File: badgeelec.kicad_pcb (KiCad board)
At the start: 2 copper layers, 44.9 x 43.2 mm, 29 parts, among them J1 PROG_CONN, U1 PIC16F716-I-SO-ND, U2 TSSP58038

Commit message: additional details
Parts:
- moved C1 61.5 mm to (159.4, 100.3)
- moved C2 61.5 mm to (159.4, 104.1)
- moved C3 61.5 mm to (131.4, 106.0)
- moved D1 61.5 mm to (157.5, 81.3)
- moved D3 61.5 mm to (157.5, 85.1)
- moved D5 61.5 mm to (141.6, 81.3)
- moved D7 61.5 mm to (141.6, 85.1)
- moved R1 61.5 mm to (157.5, 91.4)
- moved R4 61.5 mm to (145.4, 91.4)
- moved U2 61.5 mm to (135.9, 109.2)
- moved BT1 61.5 mm to (151.9, 96.5)
- moved D2 61.5 mm to (162.6, 81.3)
- moved D4 61.5 mm to (162.6, 85.1)
- moved D6 61.5 mm to (146.7, 81.3)
- moved D8 61.5 mm to (146.7, 85.1)
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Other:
- board text added: "r1"

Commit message: Halfway through v2
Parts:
- added C4, C5: 18pF, Capacitors_SMD:C_0805, F.Cu at (151.4, 128.2)
- added D10: LED, LEDs:LED_1206, F.Cu at (151.4, 128.2)
- added R6: 220, Resistors_SMD:R_0805_HandSoldering, F.Cu at (151.4, 128.2)
- added Y1: 4Mhz, Crystals:Crystal_HC49-U_Vertical, F.Cu at (162.2, 109.8)
- moved G*** 36.5 mm to (133.2, 90.0)
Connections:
- U1 pad 10: /RB4 -> (no net)
- U1 pad 11: /RB5 -> (no net)
- U1 pad 3: Net-(U1-Pad3) -> (no net)
- U1 pad 9: /RB3 -> (no net)

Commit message: Implemented prototypev2
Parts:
- removed D10: LED, LEDs:LED_1206
- removed the G*** at (133.2, 90.0)
- removed JP1: permit operation / !program, Oddities:NetTie-I_SMD
- removed R6: 220, Resistors_SMD:R_0805_HandSoldering
- removed the REF** at (170.2, 78.7)
- removed the REF** at (170.2, 114.3)
- removed the REF** at (132.7, 78.7)
- removed the REF** at (132.7, 114.3)
- added G***: LOGO, 0gbadge-2018:g22ml_small, F.Cu at (141.2, 113.8)
- added J2: PWR_CONN, Pin_Headers:Pin_Header_Straight_1x02_Pitch2.54mm, F.Cu at (153.5, 129.0)
- added REF**: MountingHole_5.5mm, Mounting_Holes:MountingHole_5.5mm, F.Cu at (151.9, 72.4)
- added REF**: MountingHole_3.2mm_M3_Pad_Via, Mounting_Holes:MountingHole_3.2mm_M3_Pad_Via, F.Cu at (170.8, 118.9)
- added REF**: MountingHole_3.2mm_M3_Pad_Via, Mounting_Holes:MountingHole_3.2mm_M3_Pad_Via, F.Cu at (132.8, 118.9)
- added REF**: MountingHole_3.2mm_M3_Pad_Via, Mounting_Holes:MountingHole_3.2mm_M3_Pad_Via, F.Cu at (170.8, 81.5)
- added REF**: MountingHole_3.2mm_M3_Pad_Via, Mounting_Holes:MountingHole_3.2mm_M3_Pad_Via, F.Cu at (132.8, 81.5)
- C2: value 4.7uF -> 1uF; moved to B.Cu
- C3: value 100nF -> 10nF
- R7: value 1K -> 33K; moved to F.Cu
- Y1: footprint Crystals:Crystal_HC49-U_Vertical -> 0gbadge-2018:ABLS-4MHZ-B2-T
- moved C5 38.2 mm to (171.9, 96.0), turned to 90 degrees
- moved C4 34.9 mm to (164.9, 96.0), turned to 90 degrees
- moved C2 27.5 mm to (135.4, 90.7), turned to 270 degrees
- moved R7 17.8 mm to (132.2, 102.4), turned to 90 degrees
- moved U2 13.6 mm to (138.6, 122.5)
- moved Y1 10.6 mm to (167.4, 100.5)
- moved S1 8.52 mm to (126.9, 101.8), turned to 270 degrees
- moved J1 8.26 mm to (177.9, 99.4)
- moved BT1 7.12 mm to (152.1, 89.4)
- moved D9 5.19 mm to (157.0, 118.8)
- moved C3 5.09 mm to (126.9, 108.2), turned to 0 degrees
- moved C1 5.07 mm to (162.7, 104.2)
- moved R8 4.19 mm to (150.7, 117.5)
- moved R2 3.94 mm to (144.3, 91.2)
- moved R3 3.32 mm to (159.2, 91.2)
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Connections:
- R7 pad 2: Net-(JP1-Pad2) -> /~MCLR
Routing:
- net VDD: track 122.0 -> 170.5 mm, vias 6 -> 8
- net GND: track 38.9 -> 9.95 mm, vias 9 -> 5
- net Net-(C5-Pad1): track 0.00 -> 20.2 mm
- net /~MCLR: track 52.9 -> 67.1 mm, vias 3 -> 1
- net Net-(U1-Pad6): track 11.3 -> 23.0 mm
- net Net-(C4-Pad1): track 0.00 -> 11.2 mm
- net Net-(JP1-Pad2): track 9.76 -> 0.00 mm
- net /RB6: track 16.3 -> 22.5 mm
- net /RA1: track 13.2 -> 7.56 mm
- net /RB7: track 16.8 -> 22.0 mm
- net /RB2: track 7.69 -> 10.6 mm
- net Net-(D2-Pad1): track 9.79 -> 12.2 mm
- net /RA0: track 13.2 -> 11.1 mm
- net /RA3: track 10.3 -> 11.2 mm
- net /RA2: track 8.53 -> 7.83 mm
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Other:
- board size 44.9 x 43.2 mm -> 62.5 x 62.5 mm
- board text added: "0x0G prototype Revision 2"
- board text added: "RESET"
- board text removed: "0x0G electrical prototype"
- board text removed: "r1"

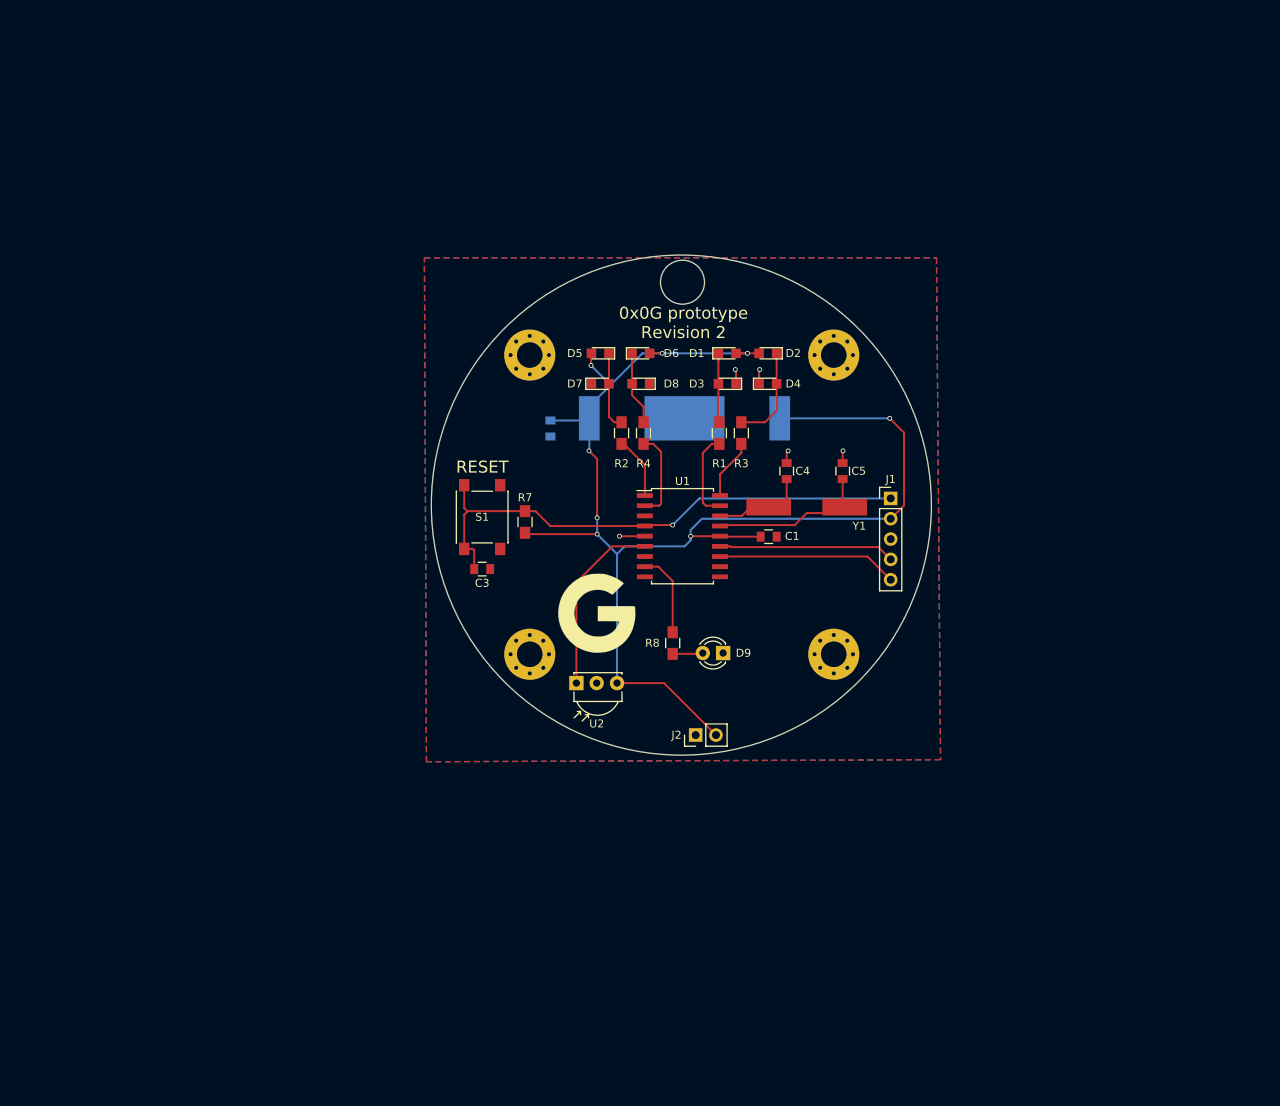
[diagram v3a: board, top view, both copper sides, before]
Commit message: Start working on layout for final prototype 1
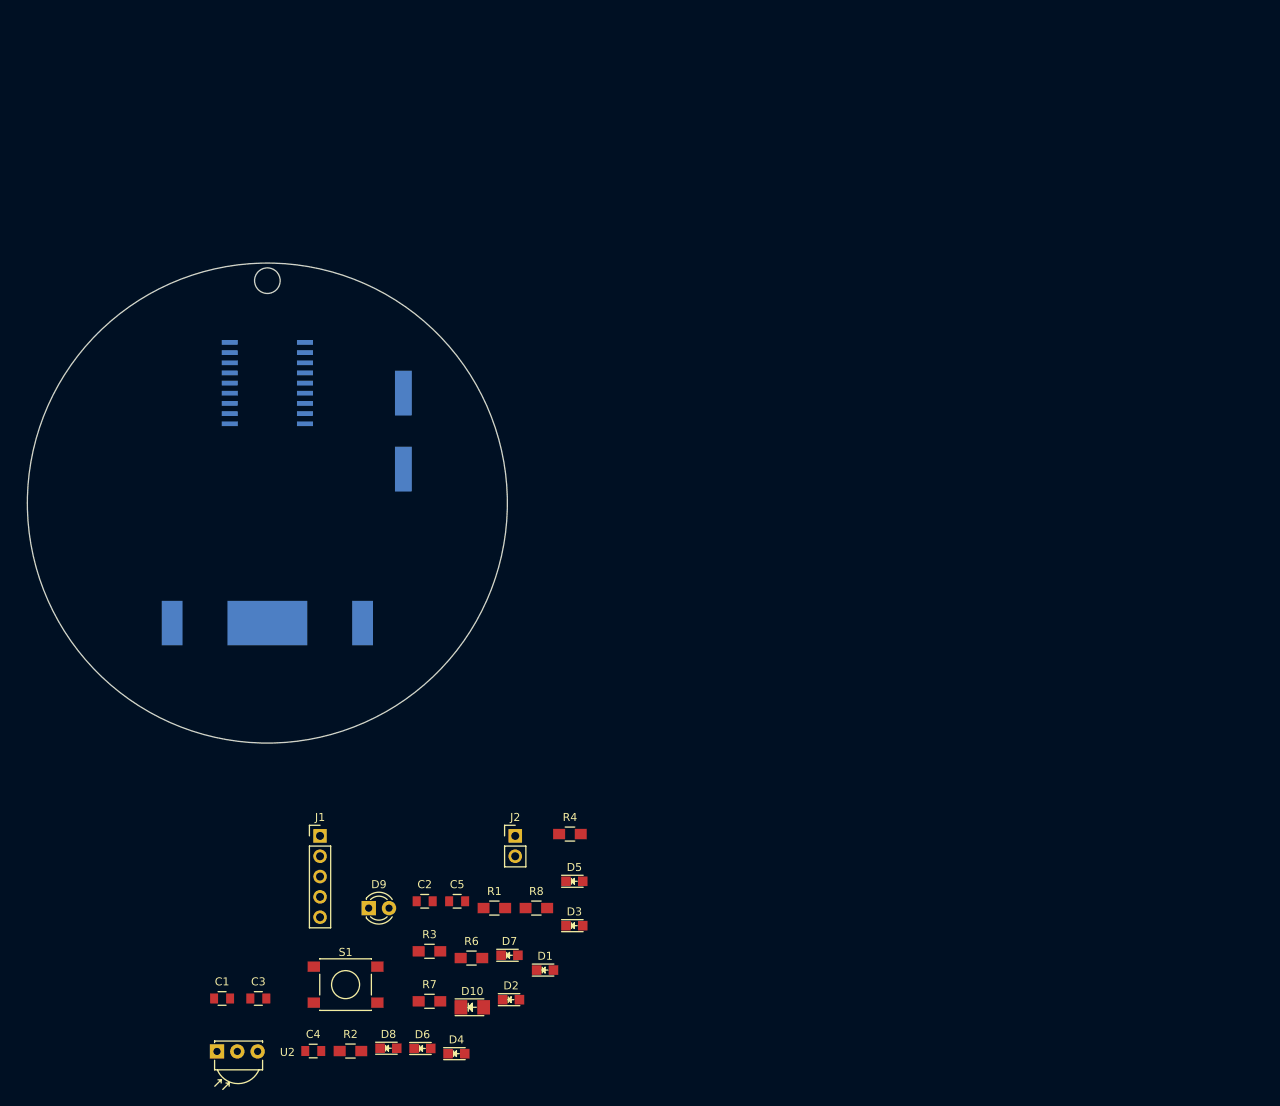
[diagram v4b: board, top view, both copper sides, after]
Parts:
- removed G***: LOGO, 0gbadge-2018:g22ml_small
- removed the REF** at (151.9, 72.4)
- removed the REF** at (170.8, 118.9)
- removed the REF** at (132.8, 118.9)
- removed the REF** at (170.8, 81.5)
- removed the REF** at (132.8, 81.5)
- added D10: LED, LEDs:LED_1206, F.Cu at (125.6, 163.0)
- added R6: 220, Resistors_SMD:R_0805_HandSoldering, F.Cu at (125.5, 156.9)
- added REF**: MountingHole_3.2mm_M3, Mounting_Holes:MountingHole_3.2mm_M3, F.Cu at (100.0, 72.2)
- C2: moved to F.Cu
- U1, Y1: moved to B.Cu
- moved C4 93.6 mm to (105.7, 168.5), turned to 0 degrees
- moved D4 92.3 mm to (123.6, 168.8)
- moved D6 91.1 mm to (119.4, 168.2)
- moved C1 89.4 mm to (94.3, 161.9)
- moved D8 88.8 mm to (115.1, 168.1), turned to 0 degrees
- moved D2 86.9 mm to (130.5, 162.1), turned to 0 degrees
- moved R2 84.4 mm to (110.4, 168.5), turned to 0 degrees
- moved J1 82.9 mm to (106.6, 141.6)
- moved D1 80.4 mm to (134.7, 158.4)
- moved R3 75.6 mm to (120.3, 156.0), turned to 0 degrees
- moved D7 72.3 mm to (130.3, 156.5)
- moved C5 72.2 mm to (123.7, 149.8), turned to 0 degrees
- moved D3 70.4 mm to (138.4, 152.8), turned to 0 degrees
- moved D5 66.1 mm to (138.4, 147.3), turned to 0 degrees
- moved R1 65.7 mm to (128.4, 150.6), turned to 0 degrees
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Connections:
- U1 pad 10: (no net) -> /RB4
- U1 pad 11: (no net) -> /RB5
- U1 pad 3: (no net) -> Net-(U1-Pad3)
- U1 pad 9: (no net) -> /RB3
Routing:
- net VDD: track 170.5 -> 0.00 mm, vias 8 -> 0
- net /~MCLR: track 67.1 -> 0.00 mm, vias 1 -> 0
- net Net-(U1-Pad6): track 23.0 -> 0.00 mm
- net /RB6: track 22.5 -> 0.00 mm
- net /RB7: track 22.0 -> 0.00 mm
- net Net-(C5-Pad1): track 20.2 -> 0.00 mm
- net Net-(D2-Pad1): track 12.2 -> 0.00 mm
- net /RA3: track 11.2 -> 0.00 mm
- net Net-(C4-Pad1): track 11.2 -> 0.00 mm
- net /RA0: track 11.1 -> 0.00 mm
- net /RB2: track 10.6 -> 0.00 mm
- net GND: track 9.95 -> 0.00 mm, vias 5 -> 0
- net Net-(D5-Pad1): track 9.86 -> 0.00 mm
- net Net-(D6-Pad1): track 9.22 -> 0.00 mm
- net Net-(D1-Pad1): track 8.84 -> 0.00 mm
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- removed copper zone on B.Cu, net GND
- removed copper zone on F.Cu, net GND
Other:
- board size 62.5 x 62.5 mm -> 60 x 60 mm
- board text removed: "0x0G prototype Revision 2"
- board text removed: "RESET"

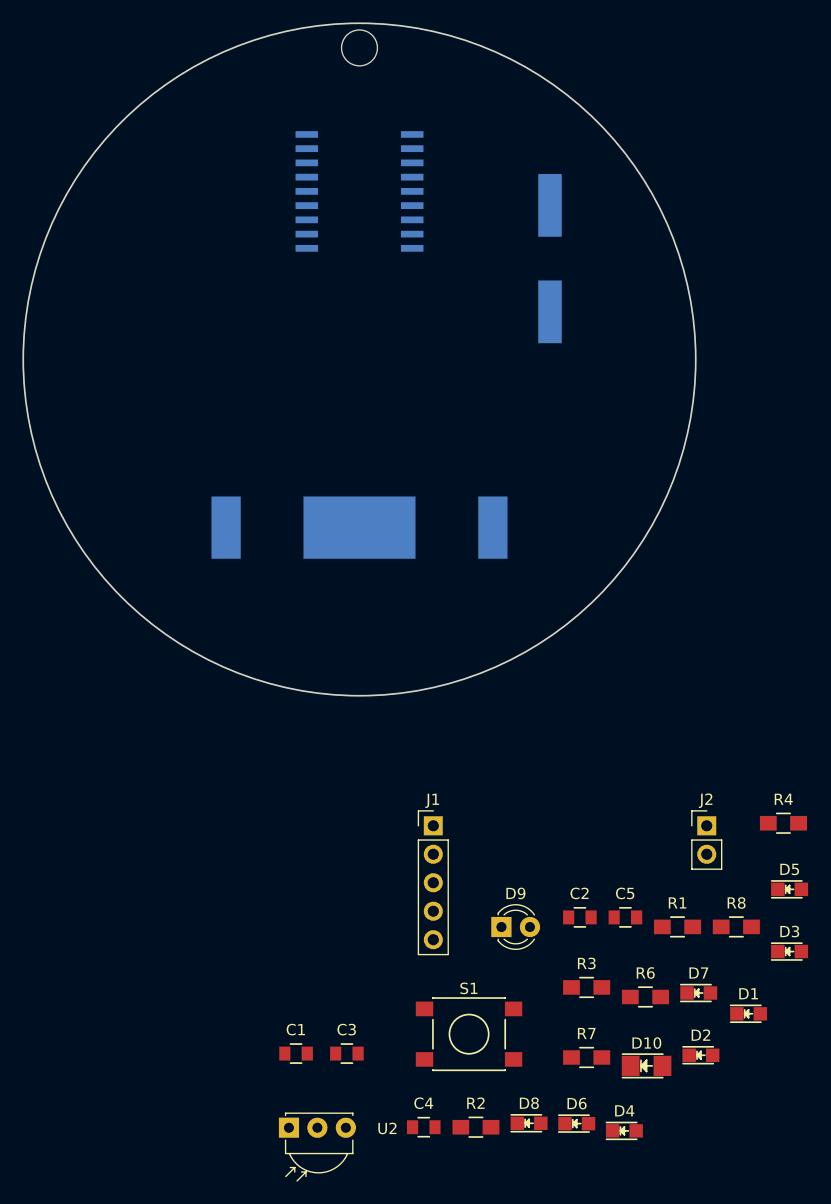
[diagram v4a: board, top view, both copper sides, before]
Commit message: Created/changed IR receiver to horizontal footprint, implemented basic generator for poker-chip style layout
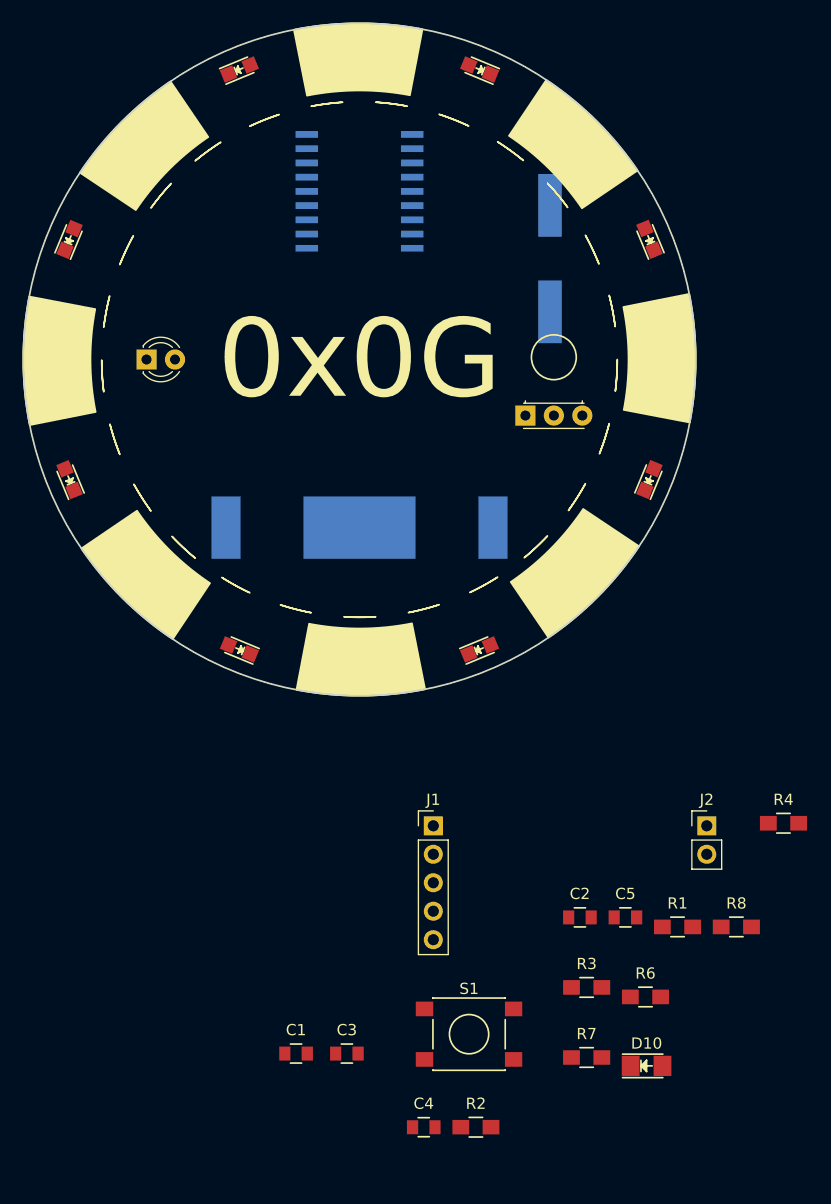
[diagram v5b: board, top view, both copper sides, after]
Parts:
- added REF**: ZEROG-GRAPHIC, graphics:graphic, F.Cu at (100.0, 100.0)
- U2: footprint Opto-Devices:IRReceiver_Vishay_MOLD-3pin -> 0gbadge-2018:tssp58038_flat
- moved D4 100.7 mm to (89.3, 74.1), turned to 22.5 degrees
- moved D2 92.0 mm to (74.1, 89.3), turned to 67.5 degrees
- moved D3 83.4 mm to (110.7, 74.1), turned to 157.5 degrees
- moved D5 73.9 mm to (74.1, 110.7), turned to 112.5 degrees
- moved D7 67.4 mm to (125.9, 89.3), turned to 112.5 degrees
- moved U2 67.0 mm to (114.8, 105.0)
- moved D9 59.7 mm to (81.0, 100.0)
- moved D6 57.8 mm to (125.9, 110.7), turned to 67.5 degrees
- moved D1 55.9 mm to (89.3, 125.9), turned to 157.5 degrees
- moved D8 42.5 mm to (110.7, 125.9), turned to 22.5 degrees
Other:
- board text added: "0x0G"

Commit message: Done layout for proto final v1
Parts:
- removed D10: LED, LEDs:LED_1206
- removed R6: 220, Resistors_SMD:R_0805_HandSoldering
- C1, C2, C4, C5, R1, R2, R3, R4, R7, R8: moved to B.Cu
- moved C1 84.0 mm to (97.0, 78.0)
- moved R3 80.2 mm to (80.0, 86.6)
- moved R1 78.7 mm to (106.3, 75.0), turned to 270 degrees
- moved C4 75.6 mm to (121.6, 94.6), turned to 90 degrees
- moved R8 74.6 mm to (83.6, 95.3), turned to 270 degrees
- moved C2 73.7 mm to (103.0, 78.0)
- moved R7 67.9 mm to (82.3, 106.0)
- moved C5 64.7 mm to (121.6, 85.1), turned to 90 degrees
- moved R2 62.8 mm to (80.1, 113.5)
- moved J1 61.0 mm to (94.9, 81.8), turned to 90 degrees
- moved C3 50.0 mm to (93.3, 112.2), turned to 90 degrees
- moved S1 49.0 mm to (100.0, 112.2)
- moved R4 33.3 mm to (119.9, 113.3), turned to 180 degrees
- moved J2 32.9 mm to (101.3, 127.6), turned to 270 degrees
- moved U1 7.00 mm to (100.0, 92.0)
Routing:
- net /~MCLR: track 0.00 -> 47.6 mm, vias 0 -> 3
- net Net-(C5-Pad1): track 0.00 -> 22.2 mm
- net Net-(C4-Pad1): track 0.00 -> 17.5 mm
- net /RB7: track 0.00 -> 12.1 mm
- net /RB6: track 0.00 -> 10.8 mm

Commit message: Routed prototype final v1
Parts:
- removed J2: PWR_CONN, Pin_Headers:Pin_Header_Straight_1x02_Pitch2.54mm
- moved R7 2.20 mm to (80.0, 106.0)
- moved R2 0.07 mm to (80.0, 113.5)
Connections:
- R3 pad 2: /RA1 -> /RB3
- U1 pad 10: /RB4 -> (no net)
- U1 pad 11: /RB5 -> (no net)
- U1 pad 18: /RA1 -> (no net)
- U1 pad 3: Net-(U1-Pad3) -> (no net)
- U1 pad 7: /RB1 -> (no net)
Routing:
- net VDD: track 0.00 -> 173.6 mm, vias 0 -> 7
- net Net-(D5-Pad1): track 0.00 -> 81.7 mm, vias 0 -> 2
- net Net-(D1-Pad1): track 0.00 -> 73.6 mm, vias 0 -> 3
- net /RA0: track 0.00 -> 46.0 mm, vias 0 -> 2
- net /RA3: track 0.00 -> 37.6 mm, vias 0 -> 2
- net Net-(D2-Pad1): track 0.00 -> 32.3 mm, vias 0 -> 2
- net Net-(U1-Pad6): track 0.00 -> 29.9 mm
- net /RA2: track 0.00 -> 27.1 mm, vias 0 -> 2
- net Net-(D6-Pad1): track 0.00 -> 22.2 mm, vias 0 -> 2
- net /~MCLR: track 47.6 -> 67.4 mm, vias 3 -> 4
- net GND: track 0.00 -> 17.2 mm, vias 0 -> 3
- net /RB2: track 0.00 -> 16.1 mm
- net /RB3: track 0.00 -> 14.0 mm
- net Net-(D9-Pad2): track 0.00 -> 3.42 mm
- added copper zone on B.Cu, net GND
- added copper zone on F.Cu, net GND
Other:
- net class Default: clearance 0.2 -> 0.17
- rule trace_clearance: 0.2 -> 0.17

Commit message: Create gerbers for r2
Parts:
- added G***: LOGO, ext_libs:prototype_33m, F.Cu at (100.0, 90.0)
